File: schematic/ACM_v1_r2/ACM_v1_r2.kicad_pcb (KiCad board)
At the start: 4 copper layers, 25.5 x 39.9 mm, 38 parts, among them J1 DF40C-60DS-0.4V(51), J2 DF40C-60DS-0.4V(51), J3 Conn_02x04_Odd_Even, J4 Conn_01x02, J5 DF40C-60DS-0.4V(51), J6 DF40C-60DS-0.4V(51), SW1 RST

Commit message: schematic and 3d assembly for opencad
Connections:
- J6 pad 22: unconnected-(J6-Pin_22-Pad22) -> /L4_IOR31A_40P
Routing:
- net /L4_IOR31A_40P: track 0.00 -> 1.68 mm, vias 0 -> 1
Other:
- board text added: "Designed in San Francisco, CA by Akiel Aries"
- board text added: "signalmesh ACM dev board v1 rev2"
- board text removed: "signalmesh ACM dev board v1 rev1 Akiel Aries"
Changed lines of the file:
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@@
 			(layers "B.Cu" "B.Mask" "B.Paste")
 			(roundrect_rratio 0.25)
-			(net "unconnected-(J6-Pin_22-Pad22)")
+			(net "/L4_IOR31A_40P")
 			(pinfunction "Pin_22_22")
 			(pintype "passive")
@@
 		)
 	)
-	(gr_text "signalmesh ACM dev board \nv1 rev1\nAkiel Aries"
+	(gr_text "signalmesh ACM dev board \nv1 rev2\n"
 		(at 130.69 89.67 270)
 		(layer "F.SilkS")
@@
 		)
 	)
+	(gr_text "Designed in San Francisco, CA\nby Akiel Aries"
+		(at 139.87 128.09 -0)
+		(layer "B.SilkS")
+		(effects
+			(font
+				(size 0.4 0.4)
+				(thickness 0.095)
+				(bold yes)
+			)
+			(justify left bottom mirror)
+		)
+	)
 	(gr_text "RST"
 		(at 155.07 123.204643 90)
@@
 	)
 	(segment
+		(start 148.24 99.68)
+		(end 149.08 99.68)
+		(width 0.1)
+		(layer "F.Cu")
+		(net "/L4_IOR31A_40P")
+	)
+	(via
+		(at 149.08 99.68)
+		(size 0.3)
+		(drill 0.2)
+		(layers "F.Cu" "B.Cu")
+		(net "/L4_IOR31A_40P")
+	)
+	(segment
+		(start 148.24 99.68)
+		(end 149.08 99.68)
+		(width 0.1)
+		(layer "B.Cu")
+		(net "/L4_IOR31A_40P")
+	)
+	(segment

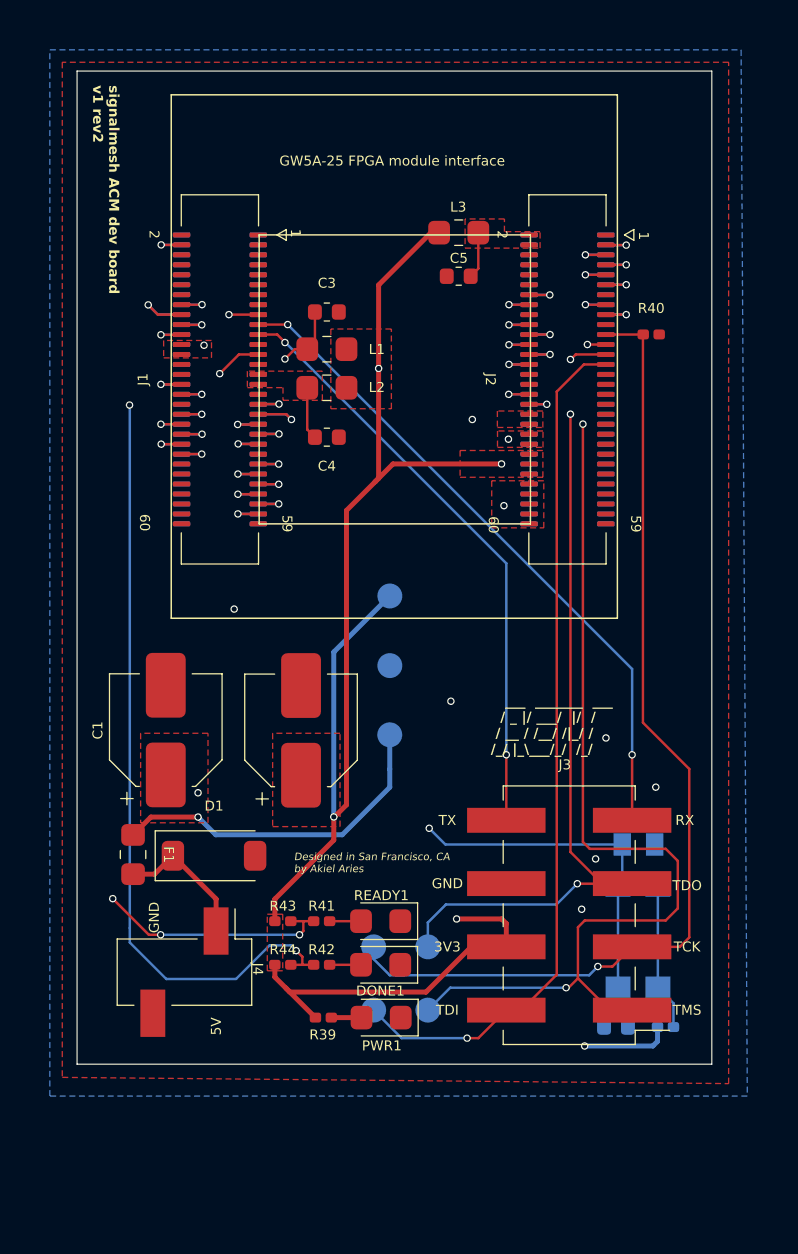
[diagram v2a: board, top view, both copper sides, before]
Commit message: im not confident the FPGA module will fit on the ACM board...
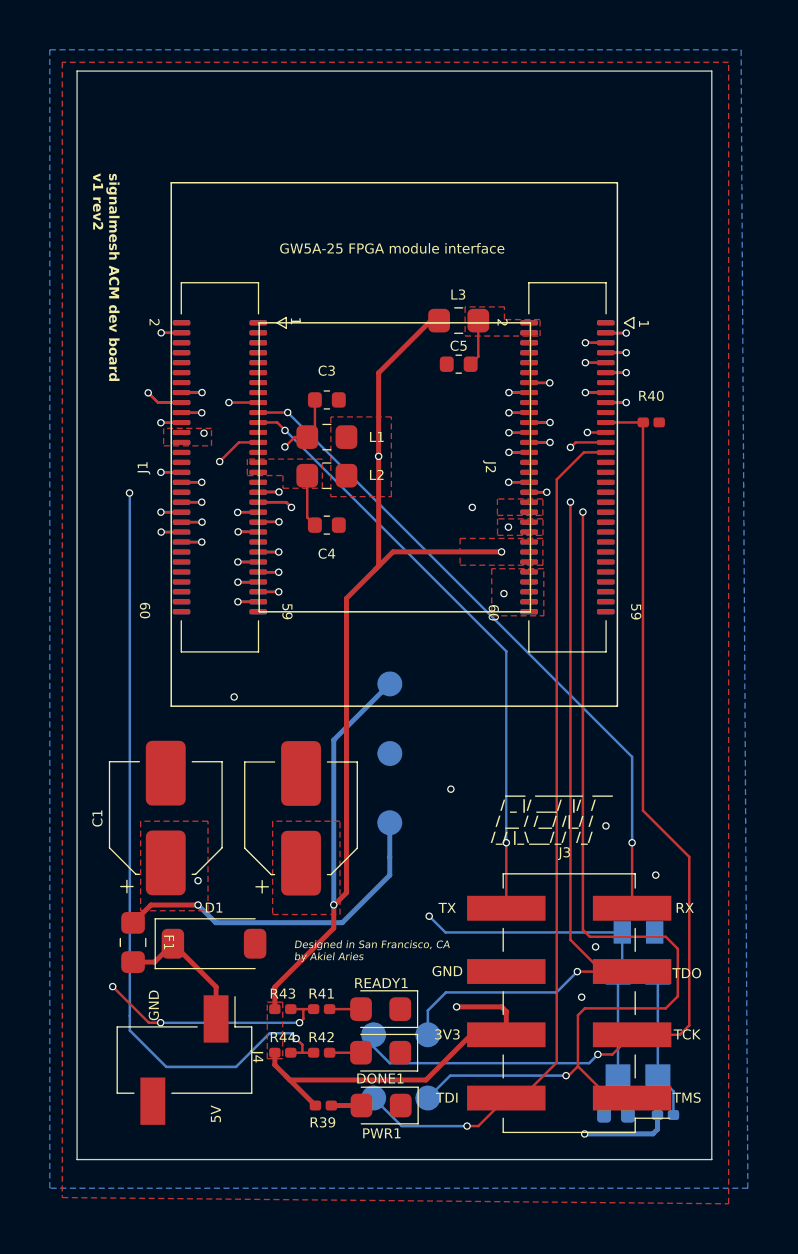
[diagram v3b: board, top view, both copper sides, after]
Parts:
- moved TDI1 3.53 mm to (142.0, 130.3)
- moved TMS1 3.53 mm to (144.2, 130.3)
- moved 3V3 3.53 mm to (142.7, 113.7)
- moved 5V1 3.53 mm to (142.6, 119.3)
- moved C1 3.53 mm to (133.7, 119.1)
- moved C2 3.53 mm to (139.1, 119.1)
- moved C3 3.53 mm to (140.1, 102.3)
- moved C4 3.53 mm to (140.1, 107.3)
- moved C5 3.53 mm to (145.4, 100.9)
- moved D1 3.53 mm to (135.6, 124.1)
- moved G*** 3.53 mm to (141.5, 118.7)
- moved GND1 3.53 mm to (142.7, 116.5)
- moved J1 3.53 mm to (135.8, 105.0)
- moved J2 3.53 mm to (149.8, 105.0)
- moved J3 3.53 mm to (149.8, 126.5)
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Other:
- board size 25.5 x 39.9 mm -> 25.5 x 43.7 mm
